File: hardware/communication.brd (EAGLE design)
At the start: 33.5 x 34.6 mm, 44 parts, among them J1 MICRO_USB_B_HIROSE_ZX62-B-5PA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, SW1 TVAF06-A020B-R, U2 NJM12888F, X1 FA-238

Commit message: Revert "communicationの層が一応完成しました。確認お願いします"
This reverts commit c7c23561daafb7c0ad8373af90d18b3355d51587.
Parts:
- removed C17: 0.1µ, rcl:C0402
- removed R10, R13: 10k, rcl:R0402
- removed R11, R12: 1k, rcl:R0402
- moved R9 40.6 mm to (-23.0, -25.4)
- moved C9 1.20 mm to (6.60, -4.06)
- moved C10 1.17 mm to (3.56, -4.06)
- moved C6 1.17 mm to (0.51, -4.06)
- moved C11 1.14 mm to (-2.54, -4.06)
- moved C14 1.14 mm to (-5.59, -4.06)
- moved C15 0.90 mm to (-8.00, 10.2)
- moved C16 0.76 mm to (-8.00, 0.25)
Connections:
- removed net CTS0: RP1.29, U$1.7
- removed net TWE_PGM: RP1.31, U$1.2
- removed net TWE_RESET: R12.1, R12.2, R13.1, RP1.32, U$1.21
- removed net TWE_SLEEP: R10.2, R11.1, R11.2, RP1.30, U$1.27
- new net SPI0_CS: RP1.32
- new net SPI0_MISO: RP1.31
- new net SPI0_MOSI: RP1.30
- new net SPI0_SCK: RP1.29
- new net SPI1_MISO: RP1.15
- new net SPI1_MOSI: RP1.18
- new net SPI1_SCK: RP1.17
- new net VCC: U$1.5
- net GND: no longer C17.1, R13.2
- net RX0: no longer U$1.8
- net TX0: no longer U$1.9
- net VDD: no longer C17.2, R10.1, U$1.5
- net WKUP: no longer RP1.15
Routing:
- net CTS0: track 49.8 -> 0.00 mm, vias 5 -> 0
- net RX0: track 57.7 -> 20.5 mm, vias 3 -> 1
- net VDD: track 137.3 -> 101.9 mm, vias 15 -> 7
- net TX0: track 58.3 -> 23.7 mm
- net TWE_SLEEP: track 31.3 -> 0.00 mm, vias 3 -> 0
- net TWE_PGM: track 27.2 -> 0.00 mm, vias 5 -> 0
- net TWE_RESET: track 24.1 -> 0.00 mm, vias 3 -> 0
- net WKUP: track 15.7 -> 0.00 mm, vias 2 -> 0
- net GND: track 185.5 -> 174.2 mm, vias 54 -> 71
- net 1V2: track 21.4 -> 19.7 mm
- net XIN1: track 10.9 -> 10.2 mm

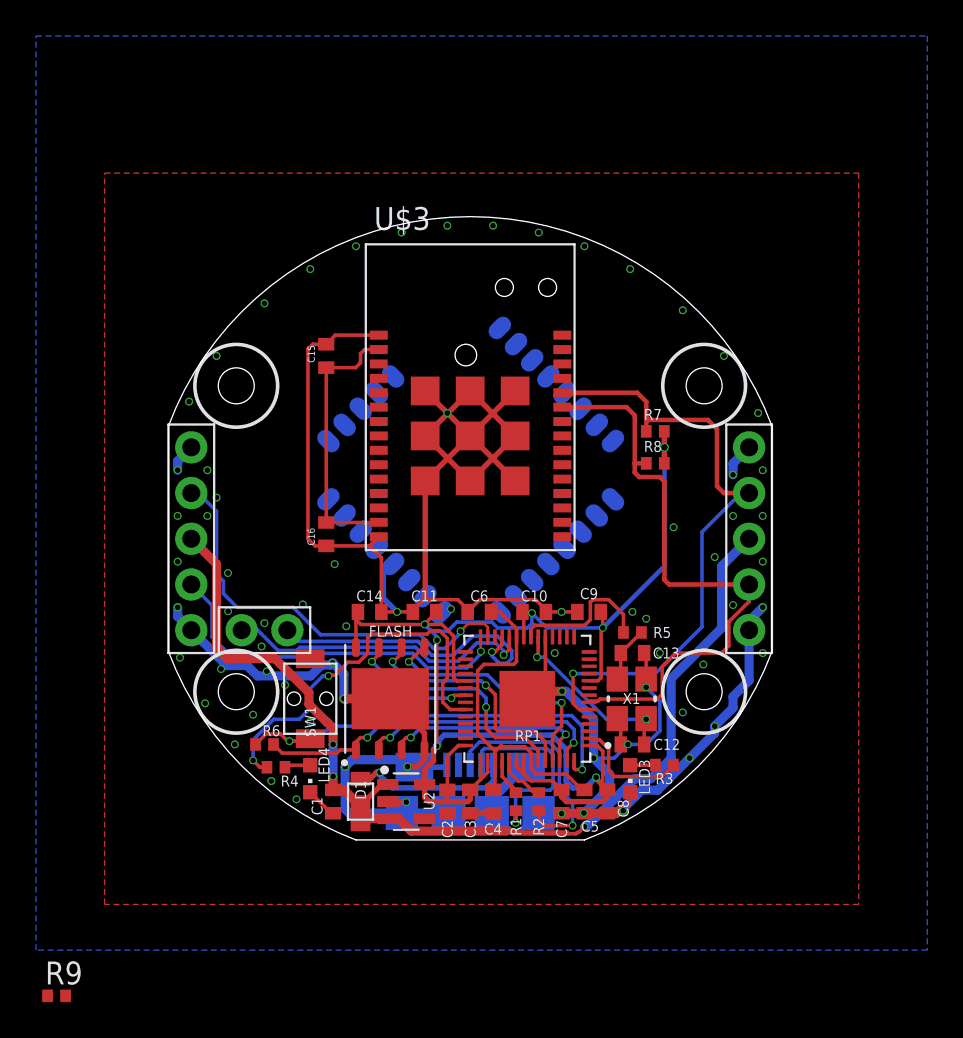
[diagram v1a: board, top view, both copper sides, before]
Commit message: communicationの層が一応完成しました。確認お願いします
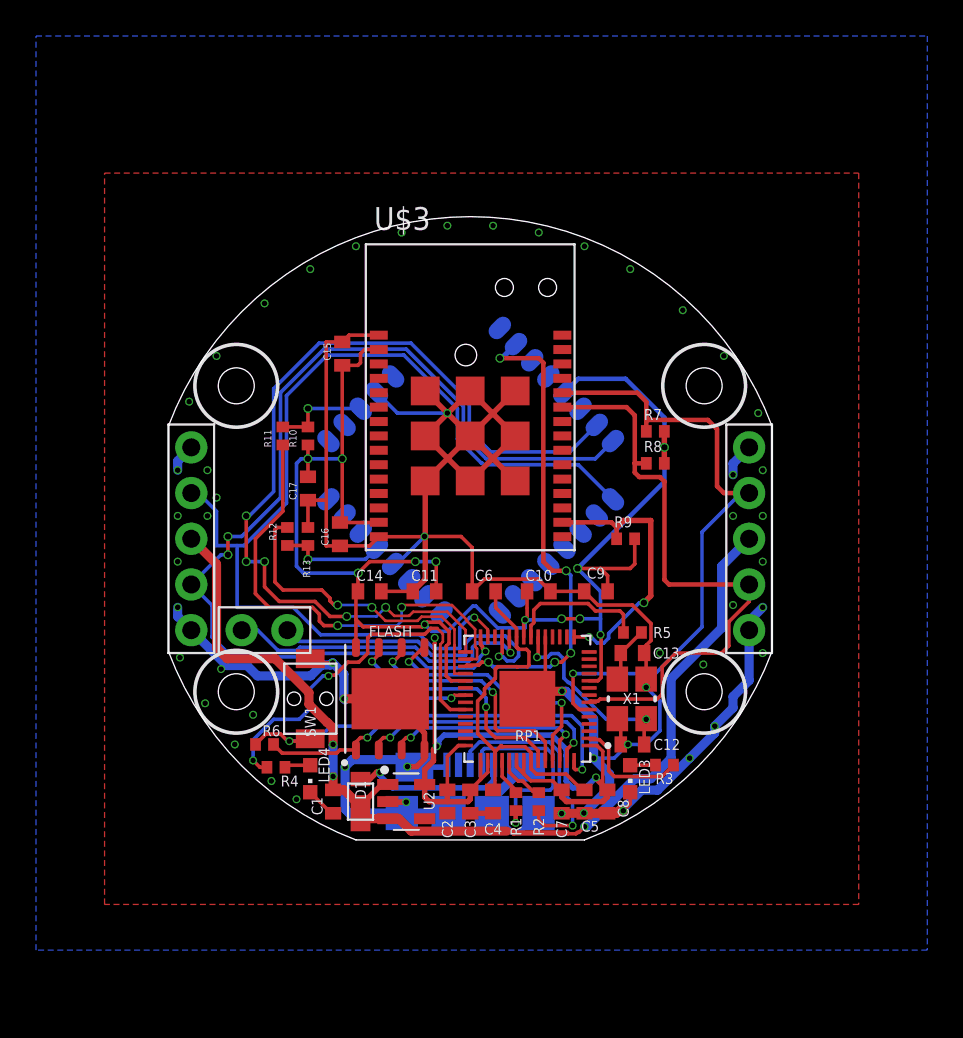
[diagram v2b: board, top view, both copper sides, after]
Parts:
- added C17: 0.1µ, rcl:C0402
- added R10, R13: 10k, rcl:R0402
- added R11, R12: 1k, rcl:R0402
- moved R9 40.6 mm to (8.64, 0.00)
- moved C9 1.20 mm to (6.99, -2.92)
- moved C10 1.17 mm to (3.81, -2.92)
- moved C6 1.17 mm to (0.76, -2.92)
- moved C11 1.14 mm to (-2.54, -2.92)
- moved C14 1.14 mm to (-5.59, -2.92)
- moved C15 0.90 mm to (-7.11, 10.3)
- moved C16 0.76 mm to (-7.24, 0.25)
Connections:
- removed net SPI0_CS: RP1.32
- removed net SPI0_MISO: RP1.31
- removed net SPI0_MOSI: RP1.30
- removed net SPI0_SCK: RP1.29
- removed net SPI1_MISO: RP1.15
- removed net SPI1_MOSI: RP1.18
- removed net SPI1_SCK: RP1.17
- removed net VCC: U$1.5
- new net CTS0: RP1.29, U$1.7
- new net TWE_PGM: RP1.31, U$1.2
- new net TWE_RESET: R12.1, R12.2, R13.1, RP1.32, U$1.21
- new net TWE_SLEEP: R10.2, R11.1, R11.2, RP1.30, U$1.27
- net GND: now also C17.1, R13.2
- net RX0: now also U$1.8
- net TX0: now also U$1.9
- net VDD: now also C17.2, R10.1, U$1.5
- net WKUP: now also RP1.15
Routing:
- net CTS0: track 0.00 -> 49.8 mm, vias 0 -> 5
- net RX0: track 20.5 -> 57.7 mm, vias 1 -> 3
- net VDD: track 101.9 -> 137.3 mm, vias 7 -> 15
- net TX0: track 23.7 -> 58.3 mm
- net TWE_SLEEP: track 0.00 -> 31.3 mm, vias 0 -> 3
- net TWE_PGM: track 0.00 -> 27.2 mm, vias 0 -> 5
- net TWE_RESET: track 0.00 -> 24.1 mm, vias 0 -> 3
- net WKUP: track 0.00 -> 15.7 mm, vias 0 -> 2
- net GND: track 174.2 -> 185.5 mm, vias 71 -> 54
- net 1V2: track 19.7 -> 21.4 mm
- net XIN1: track 10.2 -> 10.9 mm
